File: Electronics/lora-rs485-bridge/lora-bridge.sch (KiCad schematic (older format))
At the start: 45 parts, among them J1 battery, J2 ANT, J3 i2c, J4 rs485, J5 SWD, J9 USB micro, SW1 SW_Test, SW2 SW_Reset, U2 ATSAMD21G18A-AUT, U3 RFM95W-868S2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

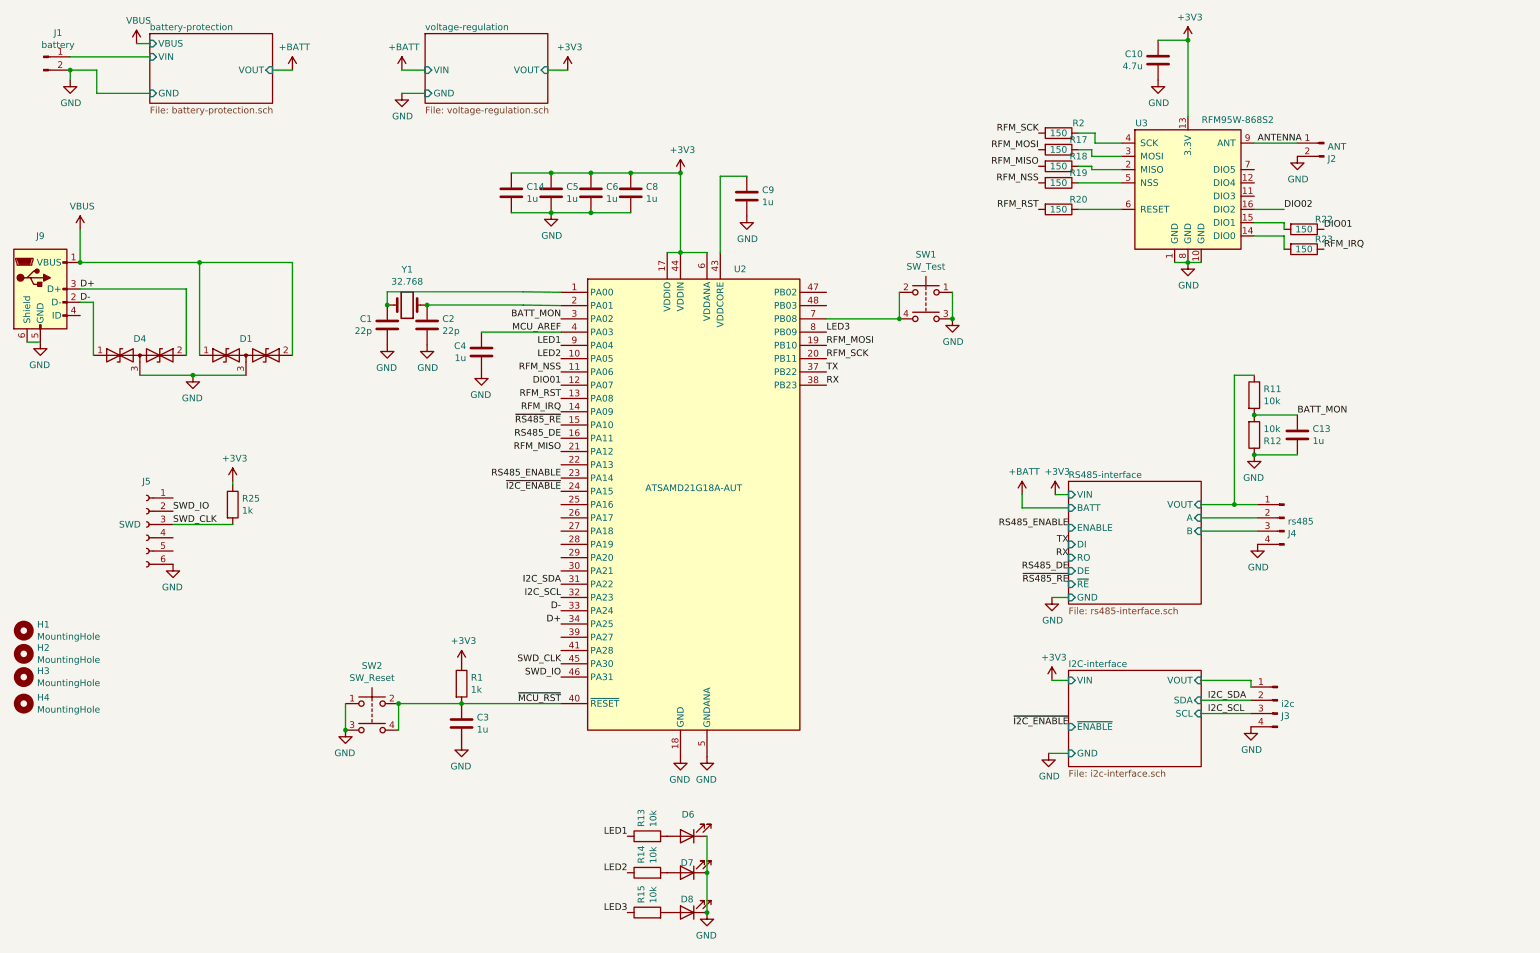
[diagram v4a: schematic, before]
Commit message: Update D3 to silicone diode as schottky leaks as hell; Add D2 to protect gates of mosfets; Remove series resistors from RFM95 interface, add pullups/downs for better sleep stability; Unify resistor values across the board; Bump version number to v1.2
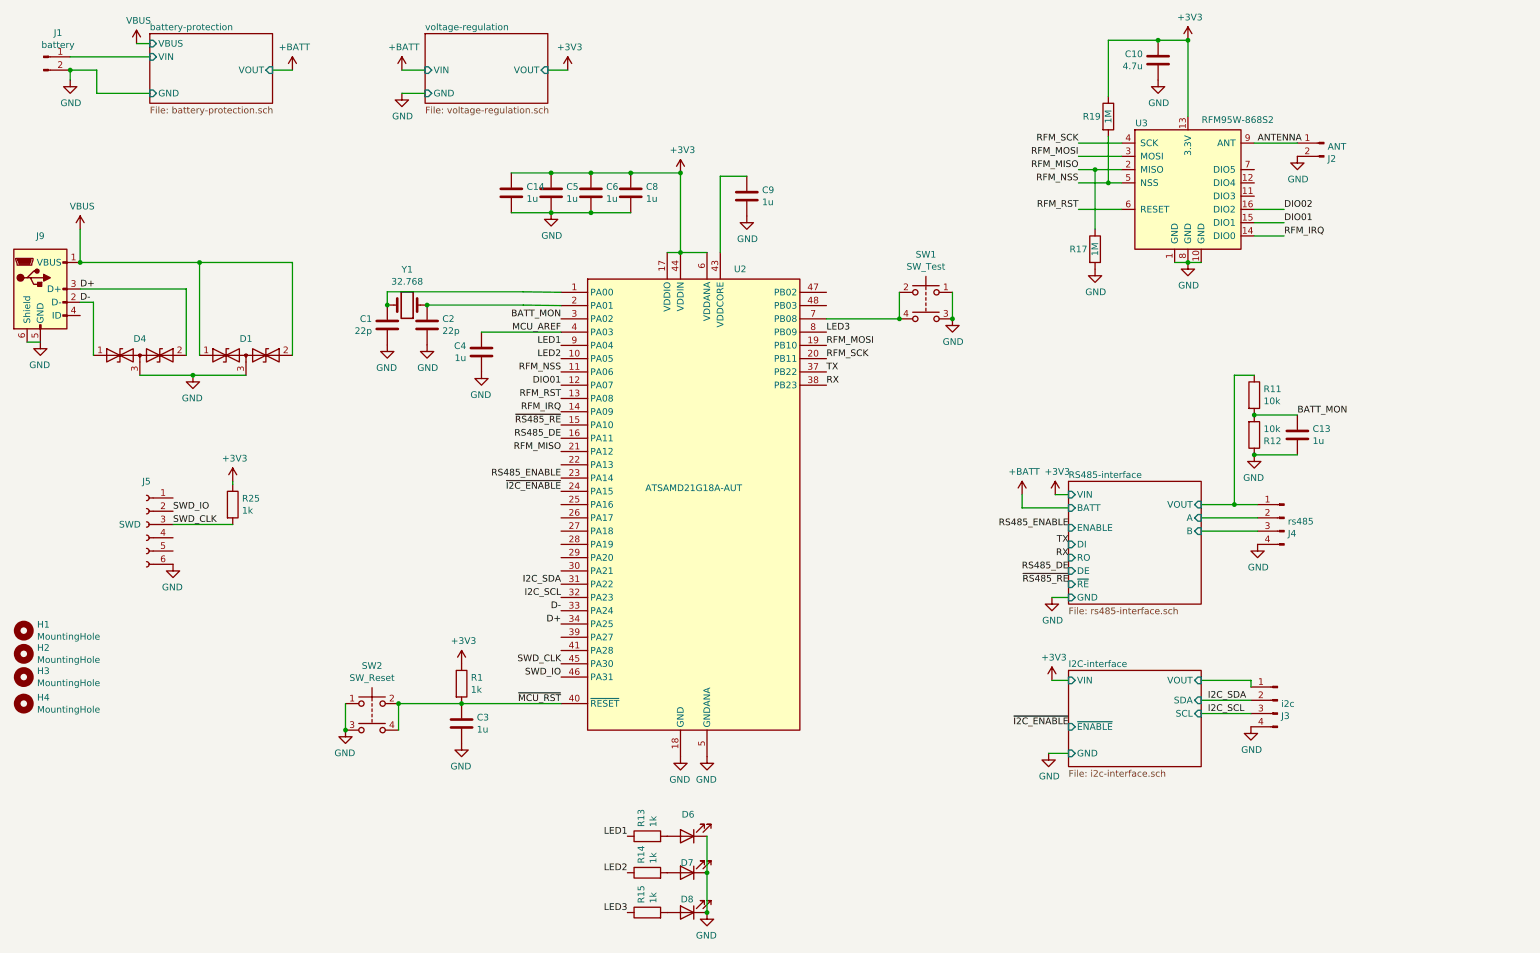
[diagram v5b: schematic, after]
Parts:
- removed R18, R2, R20, R22, R23: 150, Resistor_SMD:R_0603_1608Metric, symbol Device:R
- J2: footprint Connector_Coaxial:SMA_Amphenol_132289_EdgeMount -> miceuz-lib:SMA_6.35_EdgeMount; Comment (none) -> Can be replaced with compatible footprint connector specifi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; Manufacturer TE Connectivity AMP Connectors -> RF Solutions; PartNo 5-1814832-1 -> CON-SMA-EDGE-S
- R13, R14, R15: value 10k -> 1k
- R17, R19: value 150 -> 1M
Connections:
- net +3V3: now also R19.1
- net DIO01: now also U3.15 (DIO1)
- net GND: now also R17.2
- net RFM_IRQ: now also U3.14 (DIO0)
- net RFM_MISO: now also R17.1, U3.2 (MISO)
- net RFM_MOSI: now also U3.3 (MOSI); no longer R17.2
- net RFM_NSS: now also U3.5 (NSS)
- net RFM_RST: now also U3.6 (RESET)
- net RFM_SCK: now also U3.4 (SCK)
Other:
- moved on the sheet: R17, R19

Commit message: Move R11 and accompanying components a bit so it's easier to replace it. Add fiducials. Generate gerbers for v1.2
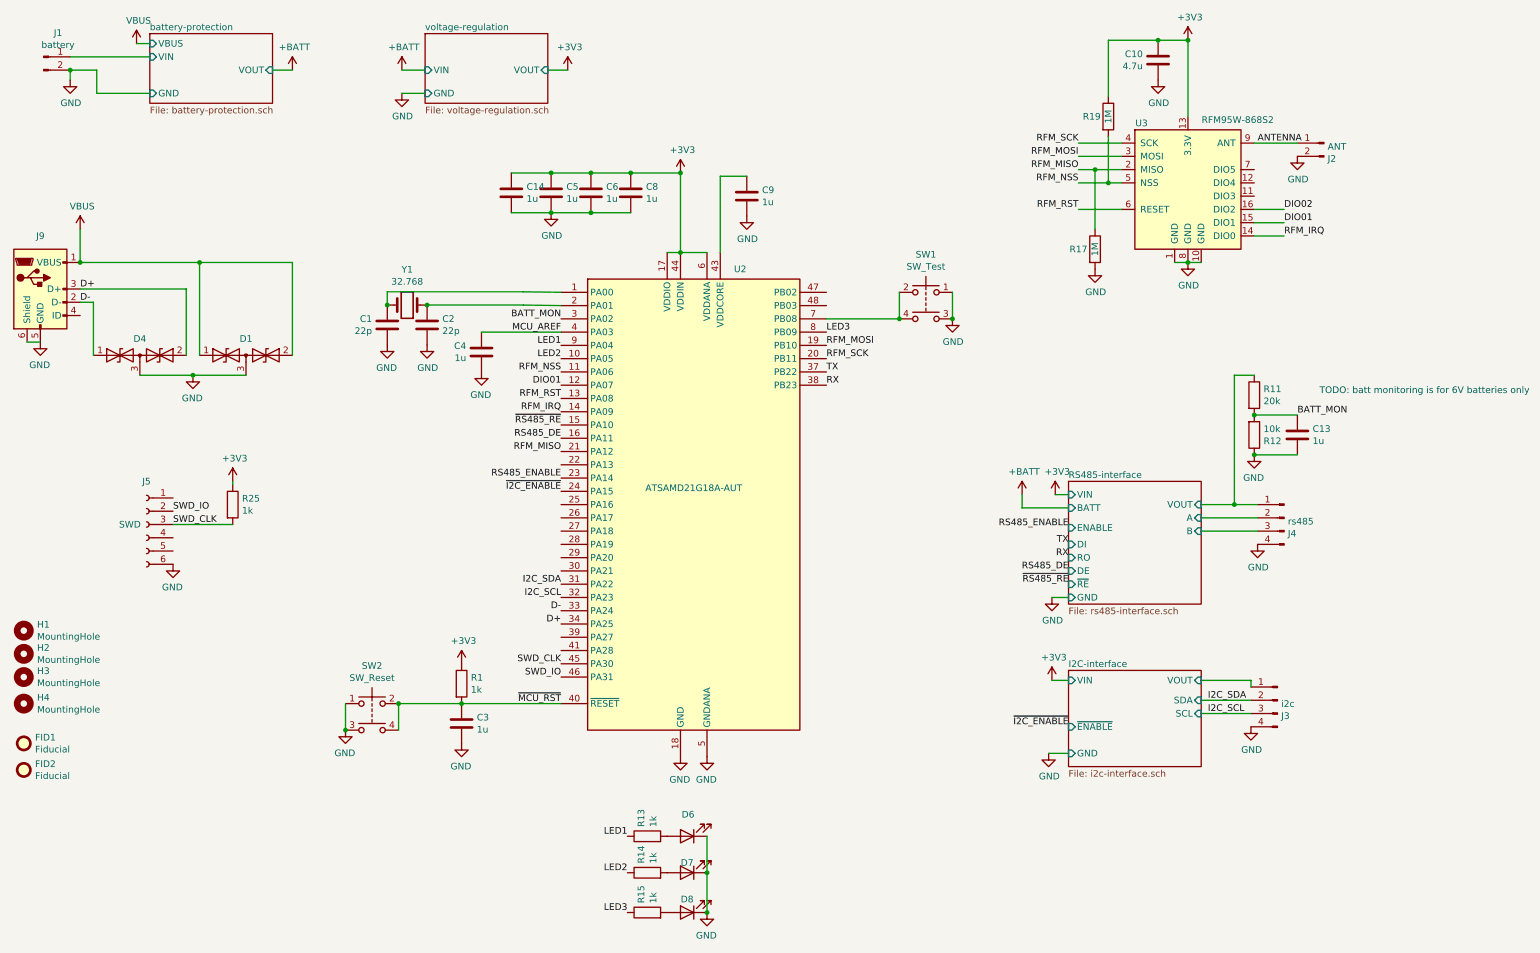
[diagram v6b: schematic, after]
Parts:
- added FID1, FID2: Fiducial, Fiducials:Fiducial_1mm_Dia_2mm_Outer, symbol Mechanical:Fiducial
- R11: value 10k -> 20k
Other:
- note added: "TODO: batt monitoring is for 6V batteries only"

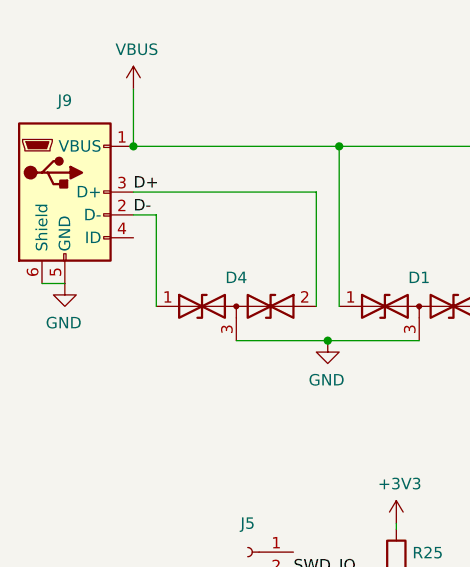
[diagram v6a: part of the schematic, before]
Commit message: Move around vias so power planes are not so much broken. Move connectors closer together so all of them are on 5.08mm grid
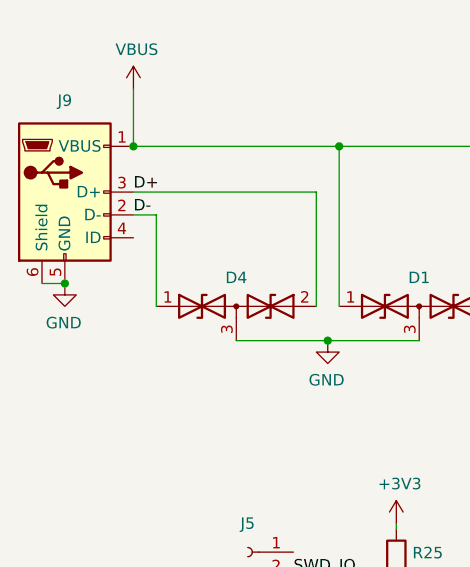
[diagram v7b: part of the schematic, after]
